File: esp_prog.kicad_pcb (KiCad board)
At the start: 2 copper layers, 29.7 x 21.1 mm, 8 parts, among them J1 10118192-0002LF, J2 Conn_01x06_Female, U1 CP2102N-A01-GQFN28, U2 SPX3819M5-L

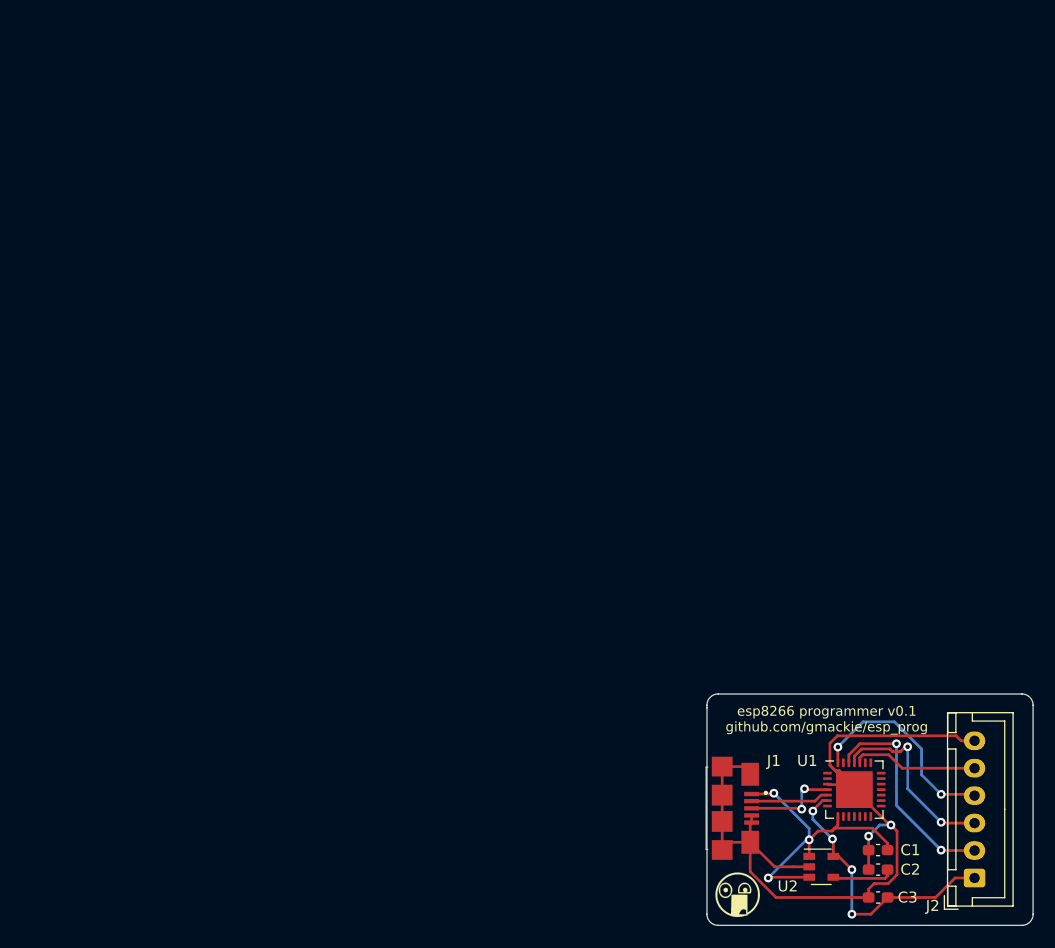
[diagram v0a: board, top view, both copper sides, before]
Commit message: v2, need to add leds and things
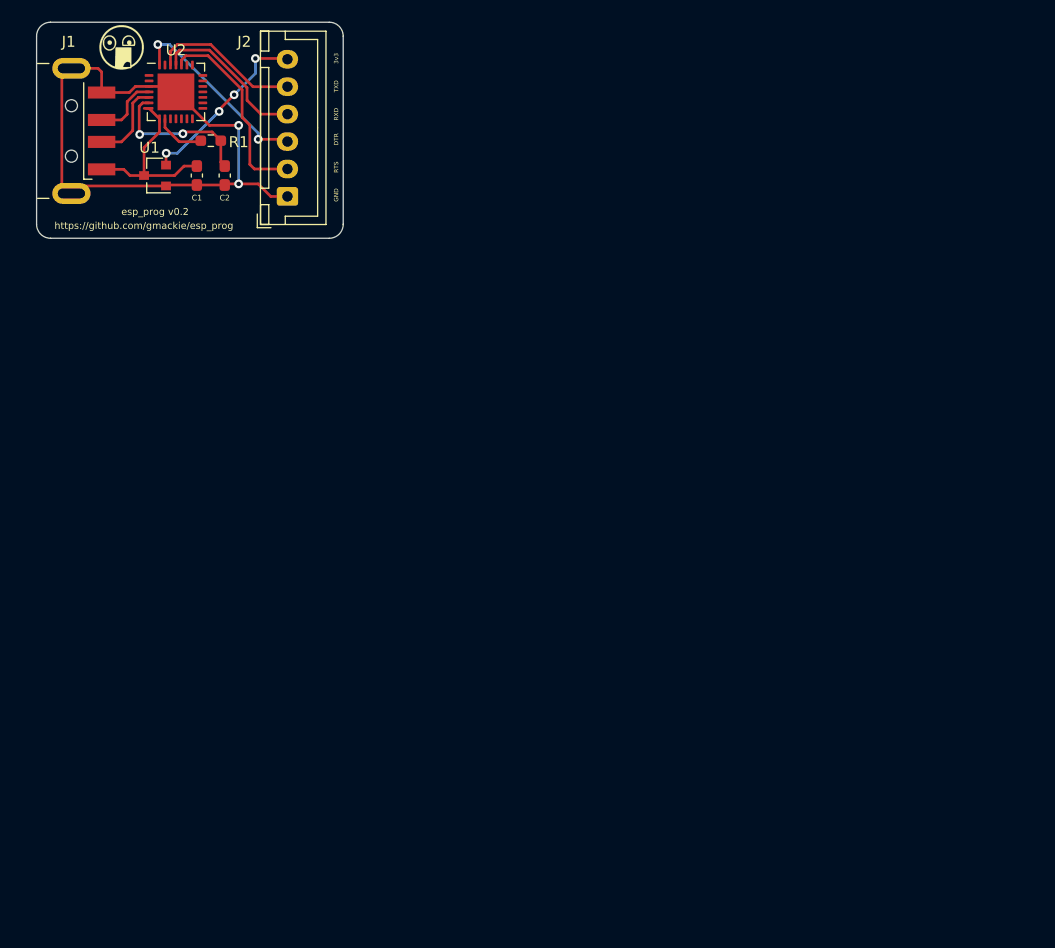
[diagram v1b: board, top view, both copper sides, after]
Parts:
- removed C3: 2.2u, Capacitor_SMD:C_0603_1608Metric_Pad1.08x0.95mm_HandSolder
- added R1: 4.7k, Resistor_SMD:R_0603_1608Metric_Pad0.98x0.95mm_HandSolder, F.Cu at (74.9, 27.3)
- C1: value 1u -> 0.1uF
- C2: value .01u -> 0.1uF
- J1: value 10118192-0002LF -> USB_A; footprint wled:AMPHENOL_10118192-0002LF -> Connector_USB:USB_A_CNCTech_1001-011-01101_Horizontal
- J2: value Conn_01x06_Female -> Conn_01x06_Male
- U1: value CP2102N-A01-GQFN28 -> MCP1700-3302E_SOT23; footprint Package_DFN_QFN:QFN-28-1EP_5x5mm_P0.5mm_EP3.35x3.35mm -> Package_TO_SOT_SMD:SOT-23
- U2: value SPX3819M5-L -> CP2102N-A01-GQFN28; footprint Package_TO_SOT_SMD:SOT-23-5 -> Package_DFN_QFN:QFN-28-1EP_5x5mm_P0.5mm_EP3.35x3.35mm
- moved G*** 95.5 mm to (66.8, 18.8)
- moved J1 92.5 mm to (55.3, 26.4), turned to 180 degrees
- moved U2 91.9 mm to (71.8, 22.9)
- moved J2 88.2 mm to (81.9, 32.4)
- moved C1 87.4 mm to (73.7, 30.5), turned to 90 degrees
- moved C2 86.9 mm to (76.2, 30.5), turned to 270 degrees
- moved U1 84.8 mm to (69.8, 30.5), turned to 180 degrees
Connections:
- C2 pad 1: GND -> VDD
- C2 pad 2: Net-(C2-Pad2) -> GND
- J2 pad 1: +3V3 -> GND
- J2 pad 2: TXD -> RTS
- J2 pad 3: RXD -> DTR
- J2 pad 4: DTR -> RXD
- J2 pad 5: RTS -> TXD
- J2 pad 6: GND -> +3V3
- U1 pad 1: (no net) -> GND
- U1 pad 2: (no net) -> +3V3
- U1 pad 3: GND -> +5V
- U2 pad 1: +5V -> (no net)
- U2 pad 2: GND -> (no net)
- U2 pad 3: +5V -> GND
- U2 pad 4: Net-(C2-Pad2) -> D+
- U2 pad 5: +3V3 -> D-
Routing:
- net GND: track 80.2 -> 56.9 mm
- net VDD: track 0.00 -> 13.9 mm, vias 0 -> 2
- net +5V: track 28.3 -> 16.8 mm, vias 3 -> 0
- net +3V3: track 25.5 -> 16.6 mm
- net RTS: track 11.5 -> 18.1 mm
- net TXD: track 19.9 -> 13.8 mm, vias 2 -> 0
- net Net-(C2-Pad2): track 5.65 -> 0.00 mm
- net Net-(R1-Pad1): track 0.00 -> 4.63 mm
- net RXD: track 17.2 -> 14.4 mm, vias 2 -> 0
- net D+: track 8.68 -> 6.05 mm, vias 2 -> 0
- net DTR: track 19.0 -> 17.7 mm
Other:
- board size 29.7 x 21.1 mm -> 27.9 x 19.7 mm
- board text added: "3v3"
- board text added: "DTR"
- board text added: "GND"
- board text added: "RTS"
- board text added: "RXD"
- board text added: "TXD"
- board text added: "esp_prog v0.2"
- board text added: "https://github.com/gmackie/esp_prog"
- board text removed: "esp8266 programmer v0.1 github.com/gmackie/esp_prog"
